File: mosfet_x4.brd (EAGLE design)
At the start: 72.1 x 30.5 mm, 26 parts, among them Q1 IRLZ34N, Q2 IRLZ34N, Q3 IRLZ34N, Q4 IRLZ34N

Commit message: Updated MOSFET board
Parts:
- moved R1 1.27 mm to (17.1, 19.7)
- moved R2 1.27 mm to (29.8, 19.7)
- moved R3 1.27 mm to (42.5, 19.7)
- moved R4 1.27 mm to (55.2, 19.7)
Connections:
- net +12V: now also X3.2; no longer X3.1
- net GND: now also X3.1; no longer X3.2
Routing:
- net +12V: track 101.3 -> 88.8 mm
- net N$1: track 8.67 -> 7.40 mm
- net N$7: track 8.67 -> 7.40 mm
- net N$3: track 8.67 -> 7.40 mm
- net N$10: track 8.67 -> 7.40 mm
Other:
- board text added: "4 channel MOSFET module v1.0 jougs@mindzoo.de"
- board text added: "GND"
- board text added: "R1-R4: 10k Q1-Q4: IRLZ34N pd_en: pull-down enable"
- board text added: "VCC C1 GND"
- board text added: "VCC C2 GND"
- board text added: "VCC C3 GND"
- board text added: "VCC C4 GND"
- board text added: "VCC GND"
- board text removed: "+ Out1 -"
- board text removed: "+ Out2 -"
- board text removed: "+ Out3 -"
- board text removed: "+ Out4 -"
- board text removed: "+ VIN -"
- board text removed: "- +"
- board text removed: "- VIN +"
- board text removed: "4 channel MOSFET module jougs@mindzoo.de"
- board text removed: "R1"
- board text removed: "R1-R4: 10k pd_en: pull down enable VOUT = VIN"
- board text removed: "R2"
- board text removed: "R3"
- board text removed: "R4"

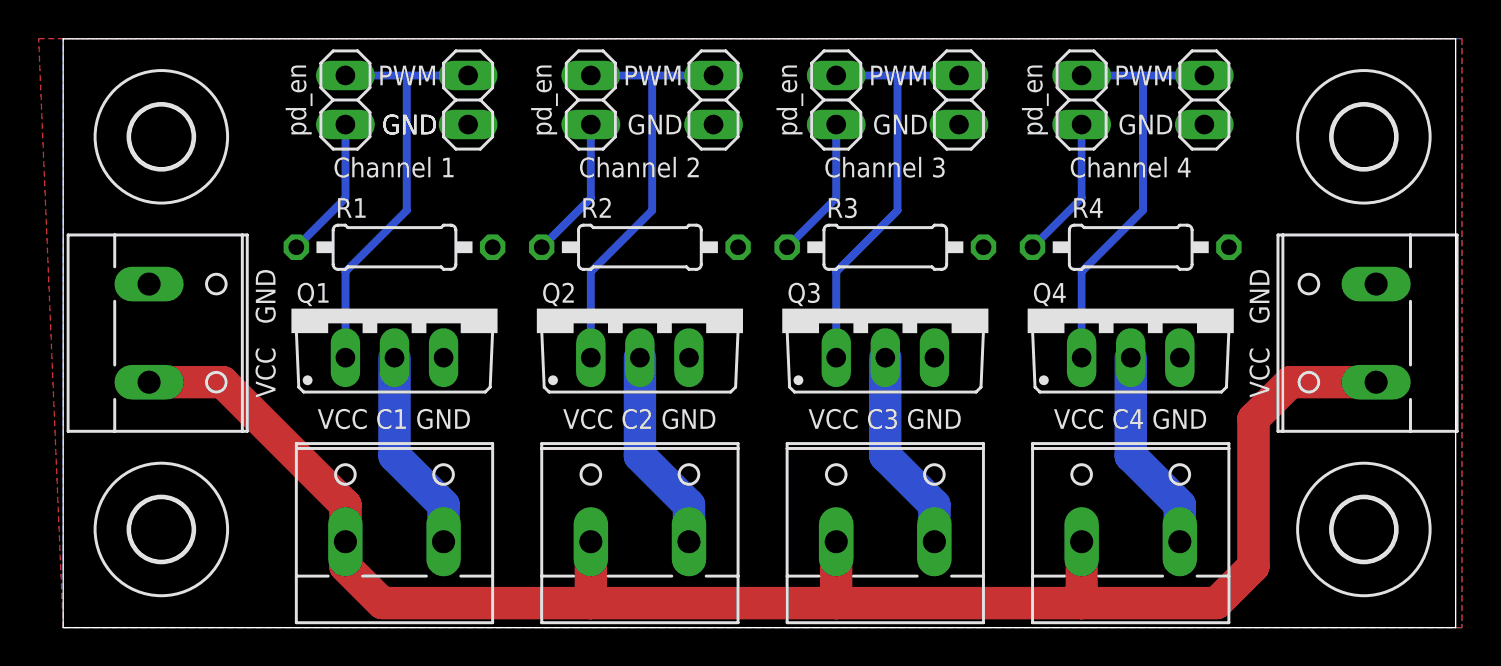
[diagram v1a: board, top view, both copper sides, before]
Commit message: Remove pulldown enable jumpers and compact and rotate connectors.
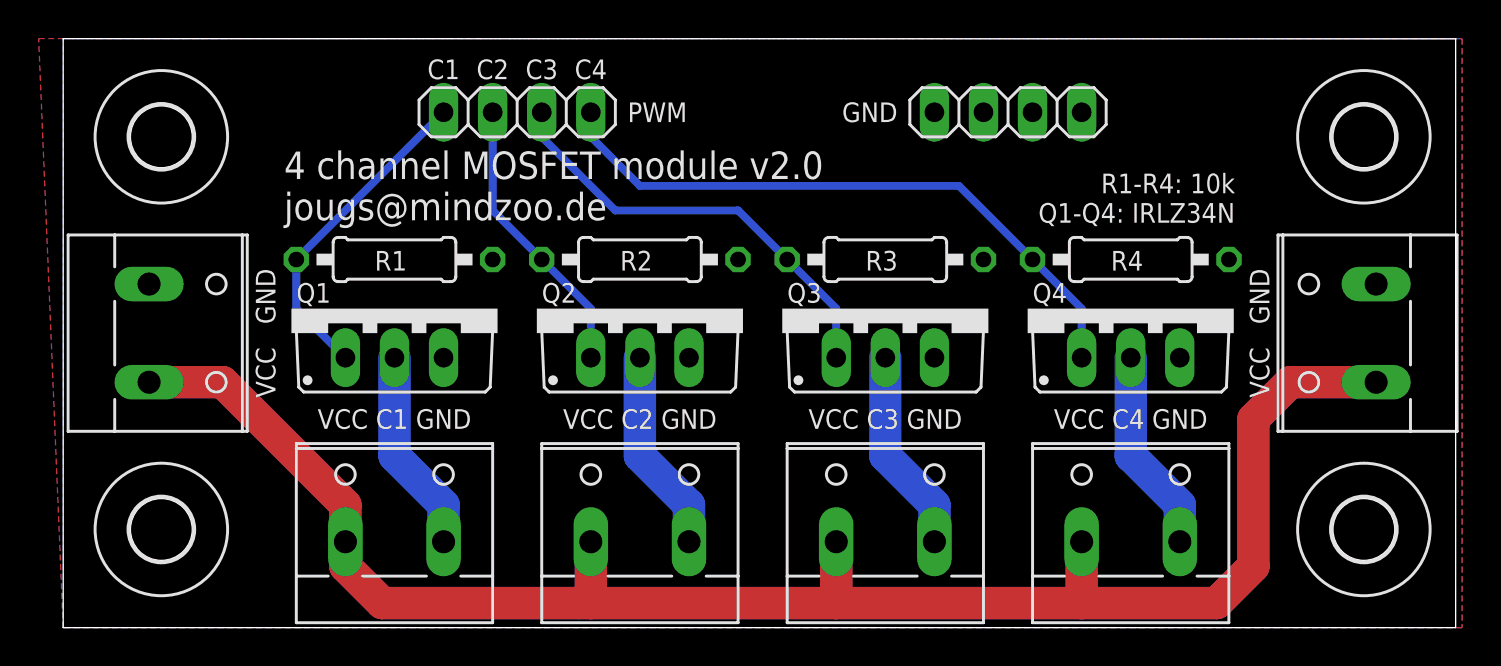
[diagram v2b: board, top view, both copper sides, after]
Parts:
- removed JP3, JP4, JP5, JP6, JP7, JP8: (no value), pinhead:1X02
- JP1, JP2: device pinhead:1X02 -> pinhead:1X04
- moved JP2 27.9 mm to (48.9, 26.7), turned to 0 degrees
- moved JP1 8.91 mm to (23.5, 26.7), turned to 180 degrees
- moved R1 0.63 mm to (17.1, 19.1)
- moved R2 0.63 mm to (29.8, 19.1)
- moved R3 0.63 mm to (42.5, 19.1)
- moved R4 0.63 mm to (55.2, 19.1)
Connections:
- removed net N$1: JP1.1, R1.2
- removed net N$10: JP7.1, R4.2
- removed net N$11: JP7.2, JP8.2, Q4.G
- removed net N$2: JP1.2, JP2.2, Q1.G
- removed net N$3: JP3.1, R2.2
- removed net N$4: JP3.2, JP4.2, Q2.G
- removed net N$7: JP5.1, R3.2
- removed net N$8: JP5.2, JP6.2, Q3.G
- new net PWM1: JP1.4, Q1.G, R1.2
- new net PWM2: JP1.3, Q2.G, R2.2
- new net PWM3: JP1.2, Q3.G, R3.2
- new net PWM4: JP1.1, Q4.G, R4.2
- net GND: now also JP2.2, JP2.3, JP2.4; no longer JP4.1, JP6.1, JP8.1
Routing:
- net +12V: track 88.8 -> 178.9 mm
- net PWM4: track 0.00 -> 32.9 mm
- net PWM3: track 0.00 -> 22.7 mm
- net N$11: track 22.3 -> 0.00 mm
- net N$4: track 22.3 -> 0.00 mm
- net N$2: track 22.3 -> 0.00 mm
- net N$8: track 22.3 -> 0.00 mm
- net PWM1: track 0.00 -> 16.9 mm
- net PWM2: track 0.00 -> 14.8 mm
- net N$1: track 7.40 -> 0.00 mm
- net N$7: track 7.40 -> 0.00 mm
- net N$3: track 7.40 -> 0.00 mm
- net N$10: track 7.40 -> 0.00 mm
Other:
- board text added: "4 channel MOSFET module v2.0 jougs@mindzoo.de"
- board text added: "C1"
- board text added: "C2"
- board text added: "C3"
- board text added: "C4"
- board text added: "R1-R4: 10k Q1-Q4: IRLZ34N"
- board text removed: "4 channel MOSFET module v1.0 jougs@mindzoo.de"
- board text removed: "Channel 1"
- board text removed: "Channel 2"
- board text removed: "Channel 3"
- board text removed: "Channel 4"
- board text removed: "R1-R4: 10k Q1-Q4: IRLZ34N pd_en: pull-down enable"
- board text removed: "pd_en"
